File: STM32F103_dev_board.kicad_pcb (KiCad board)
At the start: 4 copper layers, 39.4 x 83.8 mm, 37 parts, among them IC1 TLV70233DBVR, J1 Conn_ARM_JTAG_SWD_20, J2 Conn_01x20_Pin, J3 Conn_01x20_Pin, J4 Conn_02x03_Odd_Even, J5 USB_C_Receptacle, U1 STM32F103RBTx, U4 FT232RL, Y1 8MHz, Y2 Crystal_GND23

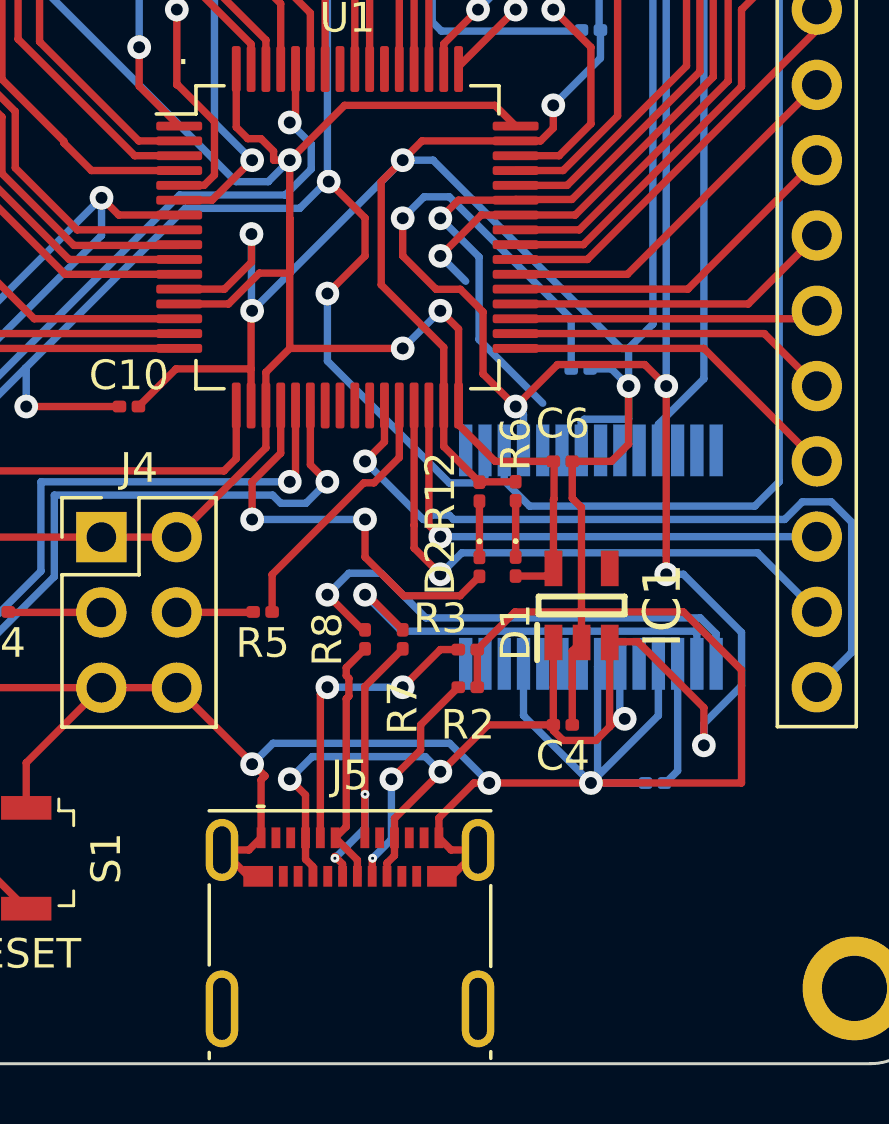
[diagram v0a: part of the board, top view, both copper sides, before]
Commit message: Changed USB C connector and fixed wiring to FT232RL
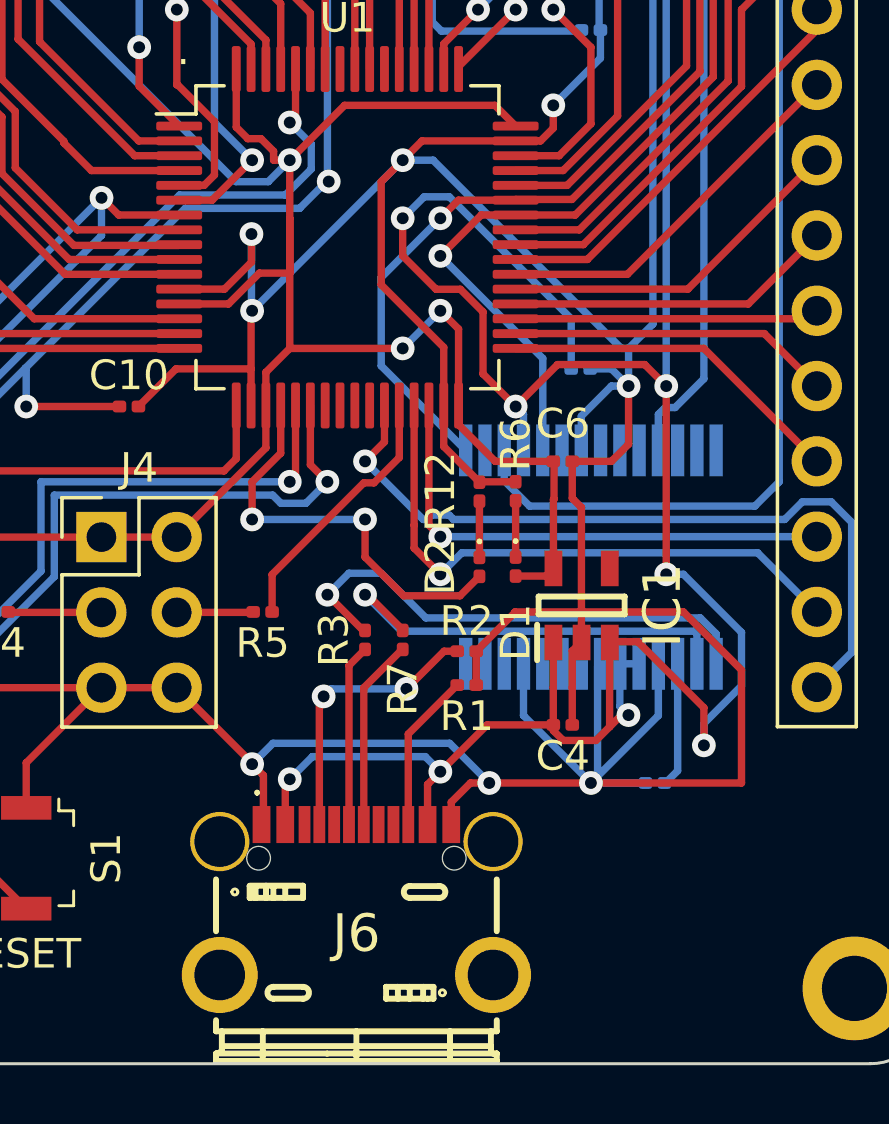
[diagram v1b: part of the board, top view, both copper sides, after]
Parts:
- removed J5: USB_C_Receptacle, Connector_USB:USB_C_Receptacle_Molex_105450-0101
- removed R8: 20, Resistor_SMD:R_0201_0603Metric
- added J6: USB4800-03-A, SamacSys_Parts:USB480003A_BIGPAD, F.Cu at (145.8, 137.2)
- added R1: 5.1k, Resistor_SMD:R_0201_0603Metric, F.Cu at (149.5, 128.8)
- R3: value 5.1k -> 20
- moved R3 3.48 mm to (146.1, 127.3), turned to 90 degrees
- moved R2 1.22 mm to (149.5, 127.6), turned to 180 degrees
- turned R7 to 90 degrees
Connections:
- R2 pad 1: Net-(J5-CC2) -> /GND
- R2 pad 2: /GND -> Net-(J6-CC1)
- R3 pad 2: /GND -> /USBDP
- R7 pad 1: /USBDM -> Net-(J6-DN1)
- R7 pad 2: Net-(J5-D--PadA7) -> /USBDM
- U4 pad 5: /PA10/USART1_RX -> /PA9/USART1_TX
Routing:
- net /RESET: track 289.0 -> 273.9 mm, vias 10 -> 9
- net Net-(J5-D--PadA7): track 10.5 -> 0.00 mm, vias 2 -> 0
- net Net-(J6-CC1): track 0.00 -> 9.52 mm, vias 0 -> 2
- net Net-(J5-D+-PadA6): track 8.48 -> 0.00 mm
- net /GND: track 315.1 -> 307.3 mm
- net Net-(J5-CC2): track 7.58 -> 0.00 mm, vias 2 -> 0
- net /PA9/USART1_TX: track 24.3 -> 31.0 mm
- net Net-(J6-DN1): track 0.00 -> 6.50 mm
- net Net-(J6-CC2): track 0.00 -> 5.39 mm
- net Net-(J6-DP1): track 10.1 -> 6.13 mm, vias 2 -> 0
- net /5V: track 108.5 -> 104.9 mm
- net /PA10/USART1_RX: track 32.4 -> 34.5 mm

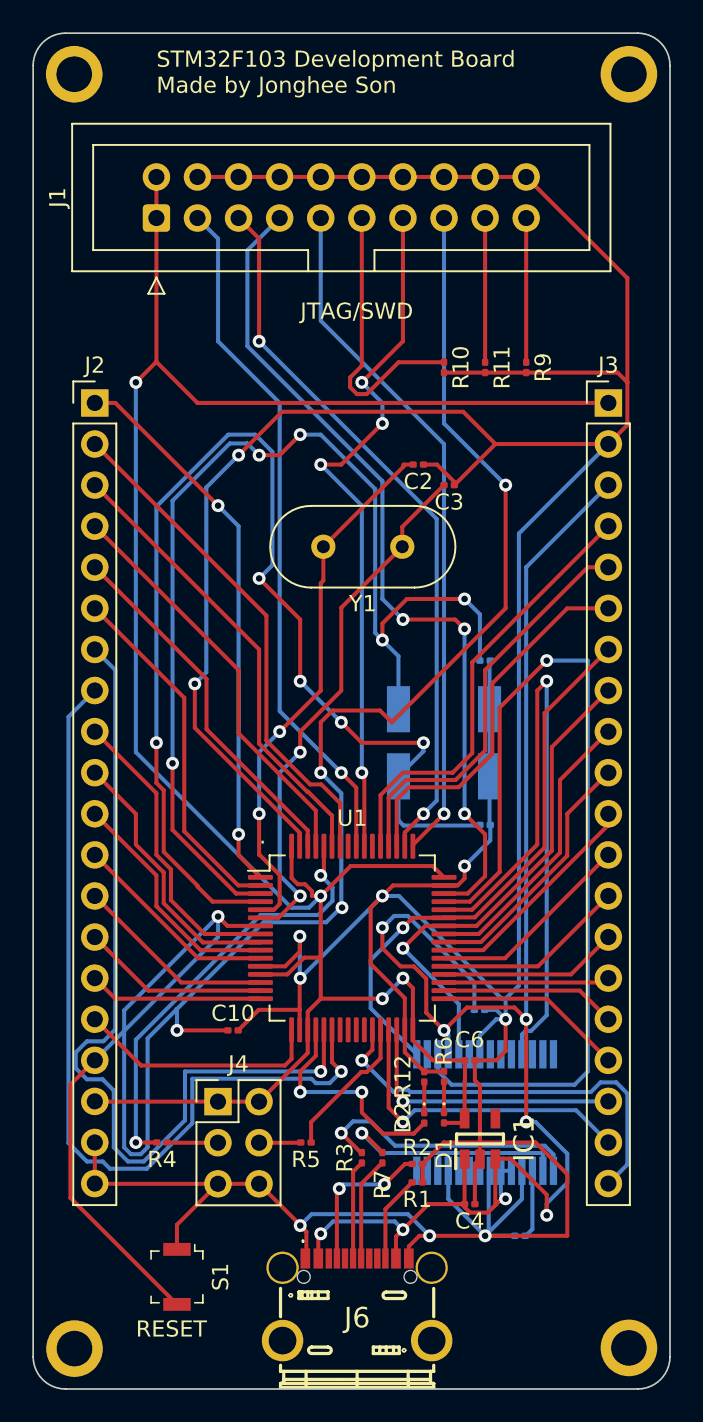
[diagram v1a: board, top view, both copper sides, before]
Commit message: Changed FT232RL into FT232RNL, fixed 32.768kHz crystal load capacitor
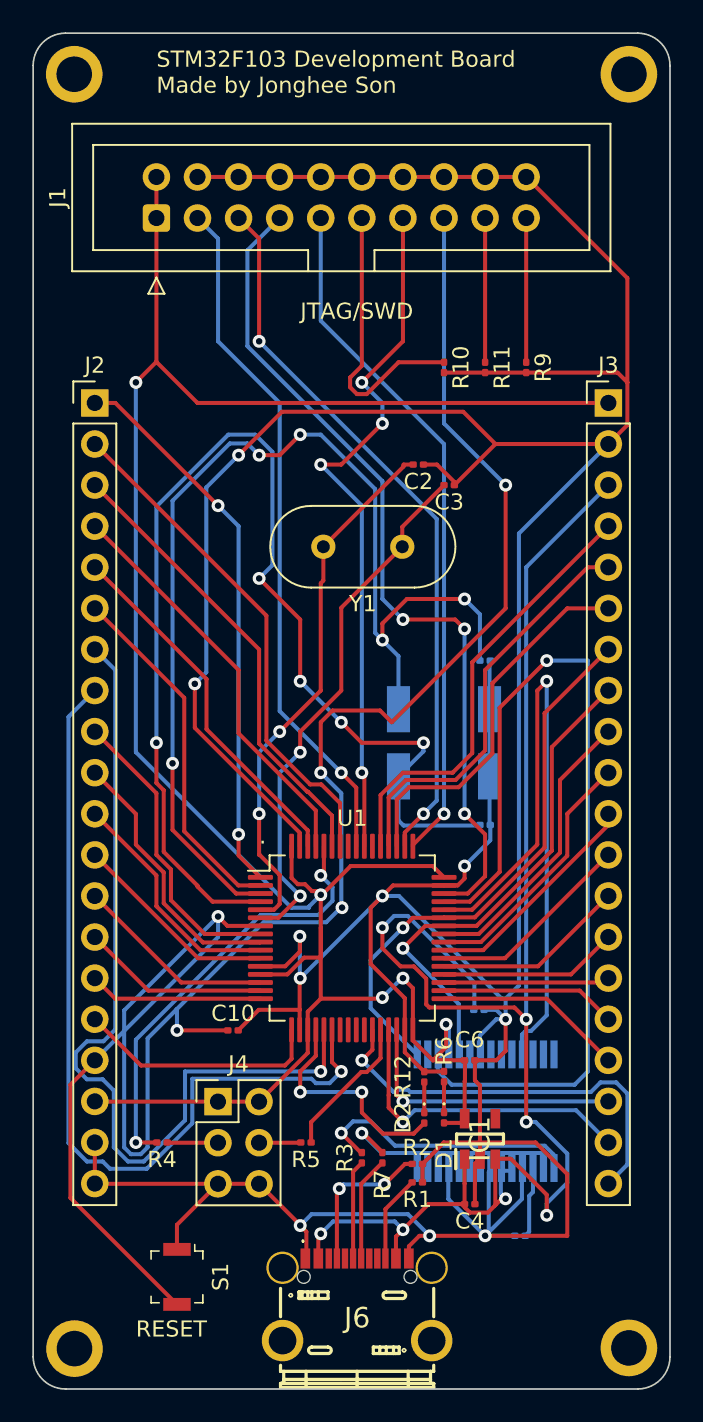
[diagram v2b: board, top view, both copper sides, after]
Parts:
- removed C8, C9: 0.1uF, Capacitor_SMD:C_0201_0603Metric
- removed U4: FT232RL, Package_SO:SSOP-28_5.3x10.2mm_P0.65mm
- added C1: 0.1uF, Capacitor_SMD:C_0201_0603Metric, B.Cu at (153.3, 118.1)
- added C5: 0.1uF, Capacitor_SMD:C_0201_0603Metric, B.Cu at (155.8, 132.1)
- added IC2: FT232RNL-REEL, SamacSys_Parts:SOP65P780X200-28N, B.Cu at (153.7, 124.4)
- C11, C12: value 22pF -> 12pF
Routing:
- net /RESET: track 273.9 -> 278.4 mm, vias 9 -> 10
- net Net-(IC2-3V3OUT): track 0.00 -> 4.39 mm
- net Net-(U4-3V3OUT): track 4.21 -> 0.00 mm
- net /5V: track 104.9 -> 101.8 mm, vias 8 -> 7

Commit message: Updated production files
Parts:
- J6: footprint SamacSys_Parts:USB480003A_BIGPAD -> SamacSys_Parts:USB480003A
